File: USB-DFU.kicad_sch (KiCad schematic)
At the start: 4 parts, among them J2 USB_C_Receptacle_USB2.0_14P, U5 USBLC6-2SC6

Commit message: MOD : KiCad 8.0.1 -> 9.0.0. ADD : Codec power circuitry.
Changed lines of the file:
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@@
 (kicad_sch
-	(version 20231120)
+	(version 20250114)
 	(generator "eeschema")
-	(generator_version "8.0")
+	(generator_version "9.0")
 	(paper "A4")
 	(junction
@@
 		(shape bidirectional)
 		(at 190.5 93.98 0)
-		(fields_autoplaced yes)
 		(effects
 			(font

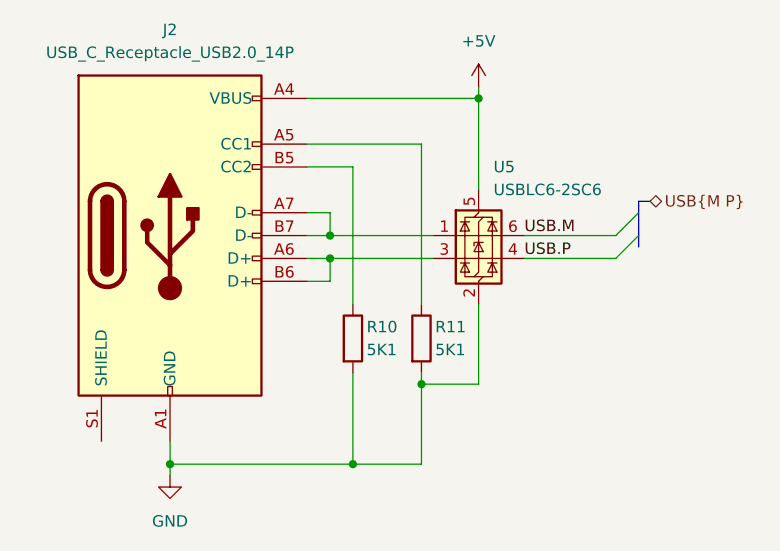
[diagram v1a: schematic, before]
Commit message: ADD : Footprint assignment. FIX : Various ERC rules.
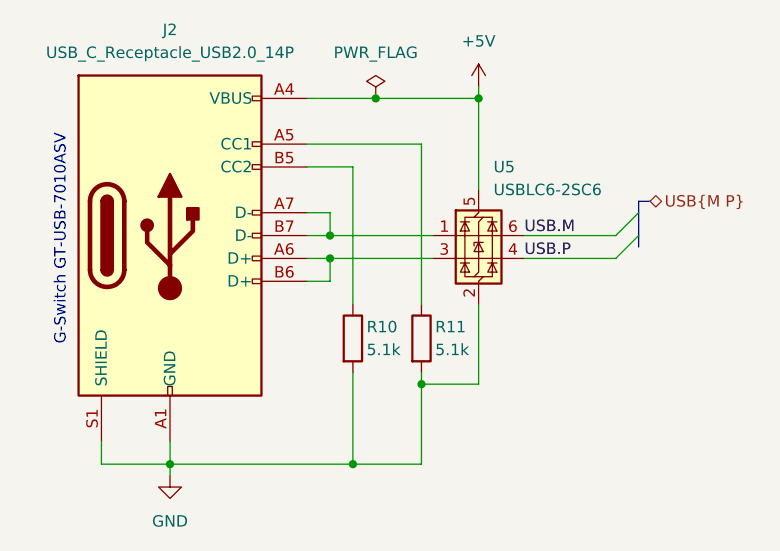
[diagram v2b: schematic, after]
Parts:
- J2: footprint (none) -> Connector_USB:USB_C_Receptacle_G-Switch_GT-USB-7010ASV
- R10, R11: value 5K1 -> 5.1k; footprint (none) -> Resistor_SMD:R_0402_1005Metric
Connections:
- net GND: now also J2.S1 (SHIELD)
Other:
- note added: "G-Switch GT-USB-7010ASV"
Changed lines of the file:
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@@
 	(generator_version "9.0")
 	(paper "A4")
+	(text "G-Switch GT-USB-7010ASV"
+		(exclude_from_sim no)
+		(at 124.968 98.298 90)
+		(effects
+			(font
+				(size 1.27 1.27)
+			)
+		)
+	)
+	(junction
+		(at 160.02 82.55)
+		(diameter 0)
+		(color 0 0 0 0)
+	)
 	(junction
 		(at 154.94 97.79)
@@
 	(wire
 		(pts
+			(xy 129.54 123.19) (xy 137.16 123.19)
+		)
+		(stroke
+			(width 0)
+			(type default)
+		)
+	)
+	(wire
+		(pts
 			(xy 154.94 97.79) (xy 152.4 97.79)
 		)
@@
 	(wire
 		(pts
-			(xy 171.45 82.55) (xy 152.4 82.55)
+			(xy 160.02 82.55) (xy 152.4 82.55)
+		)
+		(stroke
+			(width 0)
+			(type default)
+		)
+	)
+	(wire
+		(pts
+			(xy 171.45 82.55) (xy 160.02 82.55)
 		)
 		(stroke
@@
 		(pts
 			(xy 152.4 95.25) (xy 154.94 95.25)
+		)
+		(stroke
+			(width 0)
+			(type default)
+		)
+	)
+	(wire
+		(pts
+			(xy 129.54 120.65) (xy 129.54 123.19)
 		)
 		(stroke
@@
 	)
 	(symbol
+		(lib_id "power:PWR_FLAG")
+		(at 160.02 82.55 0)
+		(unit 1)
+		(exclude_from_sim no)
+		(in_bom yes)
+		(on_board yes)
+		(dnp no)
+		(fields_autoplaced yes)
+		(property "Reference" "#FLG01"
+			(at 160.02 80.645 0)
+			(effects
+				(font
+					(size 1.27 1.27)
+				)
+				(hide yes)
+			)
+		)
+		(property "Value" "PWR_FLAG"
+			(at 160.02 77.47 0)
+			(effects
+				(font
+					(size 1.27 1.27)
+				)
+			)
+		)
+		(property "Footprint" ""
+			(at 160.02 82.55 0)
+			(effects
+				(font
+					(size 1.27 1.27)
+				)
+				(hide yes)
+			)
+		)
+		(property "Datasheet" "~"
+			(at 160.02 82.55 0)
+			(effects
+				(font
+					(size 1.27 1.27)
+				)
+				(hide yes)
+			)
+		)
+		(property "Description" "Special symbol for telling ERC where power comes from"
+			(at 160.02 82.55 0)
+			(effects
+				(font
+					(size 1.27 1.27)
+				)
+				(hide yes)
+			)
+		)
+		(pin "1"
+		)
+		(instances
+			(project ""
+				(path "/d9f70aa0-fcfd-4ae4-9801-1024ce5b770a/1b8eacbf-3481-434e-abf0-0c77f2ae786c"
+					(reference "#FLG01")
+					(unit 1)
+				)
+			)
+		)
+	)
+	(symbol
 		(lib_id "Device:R")
 		(at 157.48 109.22 0)
@@
 			)
 		)
-		(property "Value" "5K1"
+		(property "Value" "5.1k"
 			(at 159.004 110.49 0)
 			(effects
@@
 			)
 		)
-		(property "Footprint" ""
+		(property "Footprint" "Resistor_SMD:R_0402_1005Metric"
 			(at 155.702 109.22 90)
 			(effects
@@
 			)
 		)
-		(property "Value" "5K1"
+		(property "Value" "5.1k"
 			(at 166.624 110.49 0)
 			(effects
@@
 			)
 		)
-		(property "Footprint" ""
+		(property "Footprint" "Resistor_SMD:R_0402_1005Metric"
 			(at 163.322 109.22 90)
 			(effects
@@
 			)
 		)
-		(property "Footprint" ""
+		(property "Footprint" "Connector_USB:USB_C_Receptacle_G-Switch_GT-USB-7010ASV"
 			(at 140.97 97.79 0)
 			(effects
